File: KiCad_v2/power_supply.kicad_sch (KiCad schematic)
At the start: 41 parts, among them U1 MT3608, U6 MCP73871, U8 TPS54331

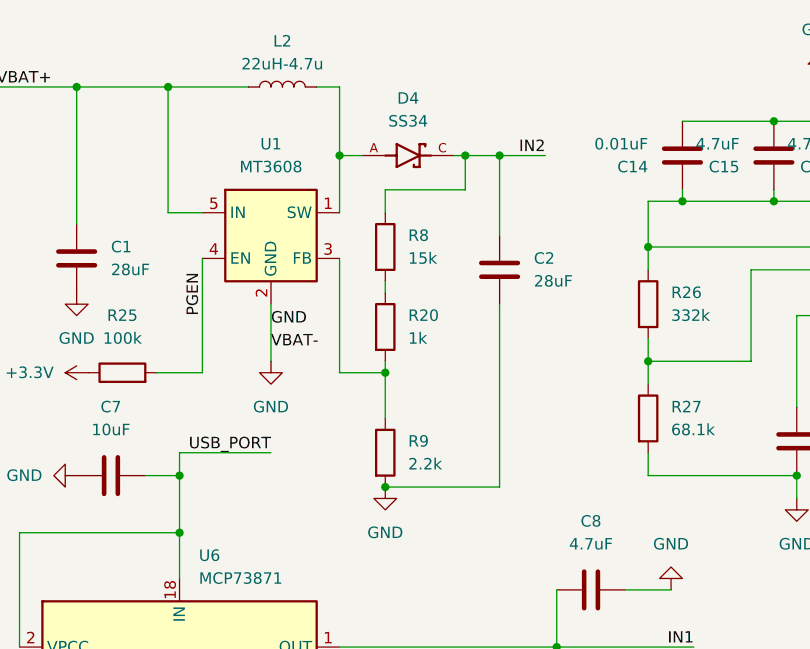
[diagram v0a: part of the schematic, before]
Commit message: feat: agrego 3d de ESP32 Y CM4
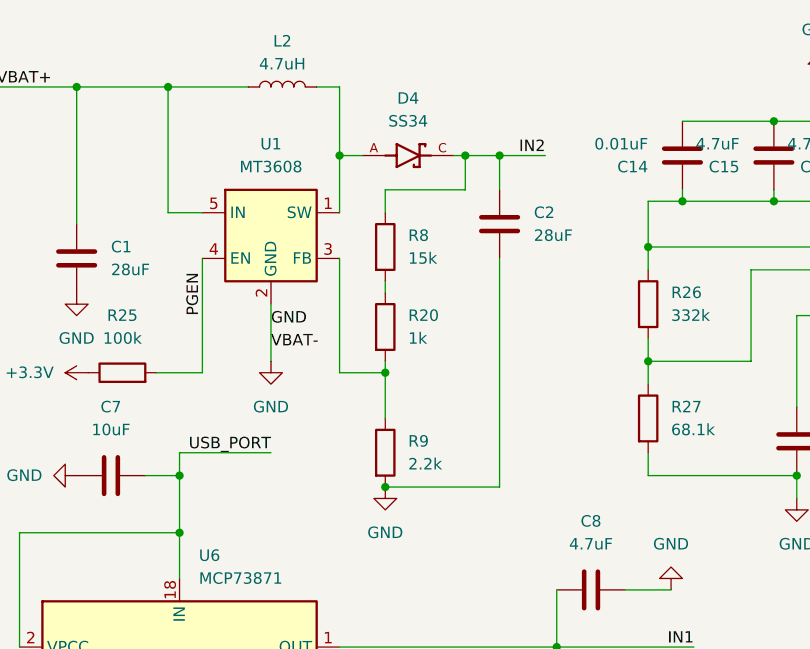
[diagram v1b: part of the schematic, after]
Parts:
- D4: footprint Footprint KiCad:DIOM7959X265N -> Custom_Footprints:DIOM7959X265N
- D5: footprint Footprint KiCad:B340A -> Custom_Footprints:B340A
- L2: value 22uH-4.7u -> 4.7uH
- U8: footprint Footprint KiCad:SOP8 -> Custom_Footprints:SOP8
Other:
- moved on the sheet: C2
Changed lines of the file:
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@@
 	(wire
 		(pts
-			(xy 109.22 88.9) (xy 109.22 109.22)
+			(xy 109.22 83.82) (xy 109.22 109.22)
 		)
 		(stroke
@@
 	(wire
 		(pts
-			(xy 109.22 72.39) (xy 109.22 81.28)
+			(xy 109.22 72.39) (xy 109.22 76.2)
 		)
 		(stroke
@@
 			)
 		)
-		(property "Footprint" "Footprint KiCad:B340A"
+		(property "Footprint" "Custom_Footprints:B340A"
 			(at 200.66 86.36 0)
 			(effects
@@
 			)
 		)
-		(property "Footprint" "Footprint KiCad:DIOM7959X265N"
+		(property "Footprint" "Custom_Footprints:DIOM7959X265N"
 			(at 99.06 72.39 0)
 			(effects
@@
 	(symbol
 		(lib_id "Device:C")
-		(at 109.22 85.09 0)
+		(at 109.22 80.01 0)
 		(unit 1)
 		(exclude_from_sim no)
@@
 		(fields_autoplaced yes)
 		(property "Reference" "C2"
-			(at 113.03 83.8199 0)
+			(at 113.03 78.7399 0)
 			(effects
 				(font
@@
 		)
 		(property "Value" "28uF"
-			(at 113.03 86.3599 0)
+			(at 113.03 81.2799 0)
 			(effects
 				(font
@@
 		)
 		(property "Footprint" "Capacitor_SMD:C_0805_2012Metric"
-			(at 110.1852 88.9 0)
+			(at 110.1852 83.82 0)
 			(effects
 				(font
@@
 		)
 		(property "Datasheet" "~"
-			(at 109.22 85.09 0)
+			(at 109.22 80.01 0)
 			(effects
 				(font
@@
 		)
 		(property "Description" "Unpolarized capacitor"
-			(at 109.22 85.09 0)
+			(at 109.22 80.01 0)
 			(effects
 				(font
@@
 		)
 		(property "Sim.Device" ""
-			(at 109.22 85.09 0)
+			(at 109.22 80.01 0)
 			(effects
 				(font
@@
 			)
 		)
-		(property "Value" "22uH-4.7u"
+		(property "Value" "4.7uH"
 			(at 85.09 62.23 90)
 			(effects
@@
 			)
 		)
-		(property "Footprint" "Footprint KiCad:SOP8"
+		(property "Footprint" "Custom_Footprints:SOP8"
 			(at 168.91 87.63 0)
 			(effects

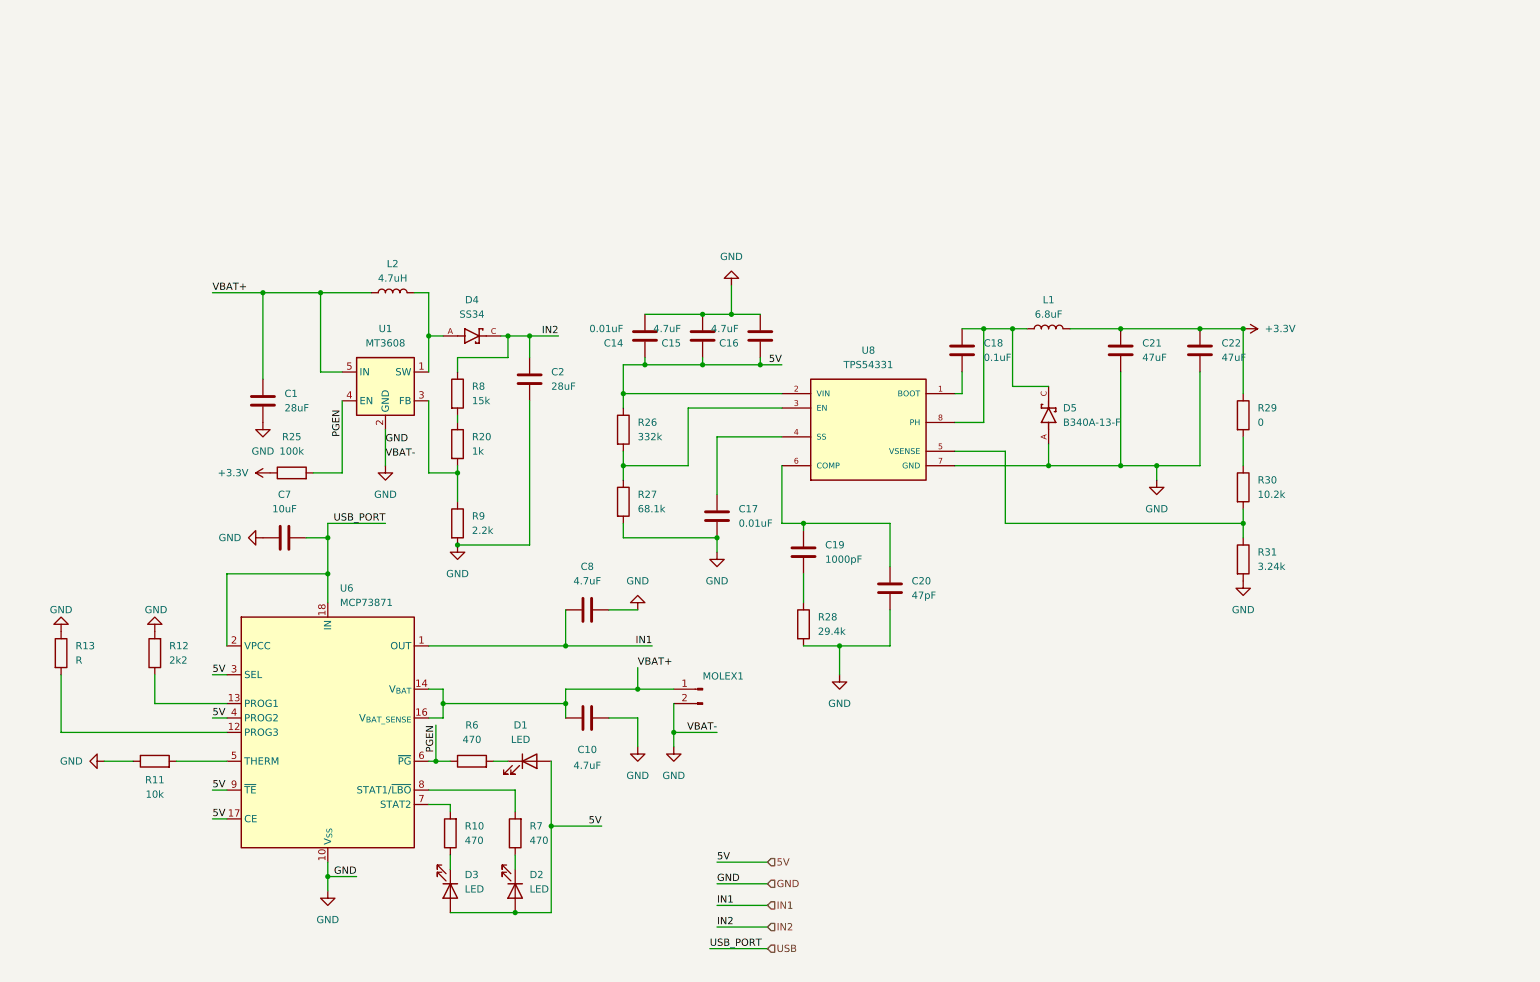
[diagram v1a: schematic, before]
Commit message: agrego step up para 3A con su debido esquematico
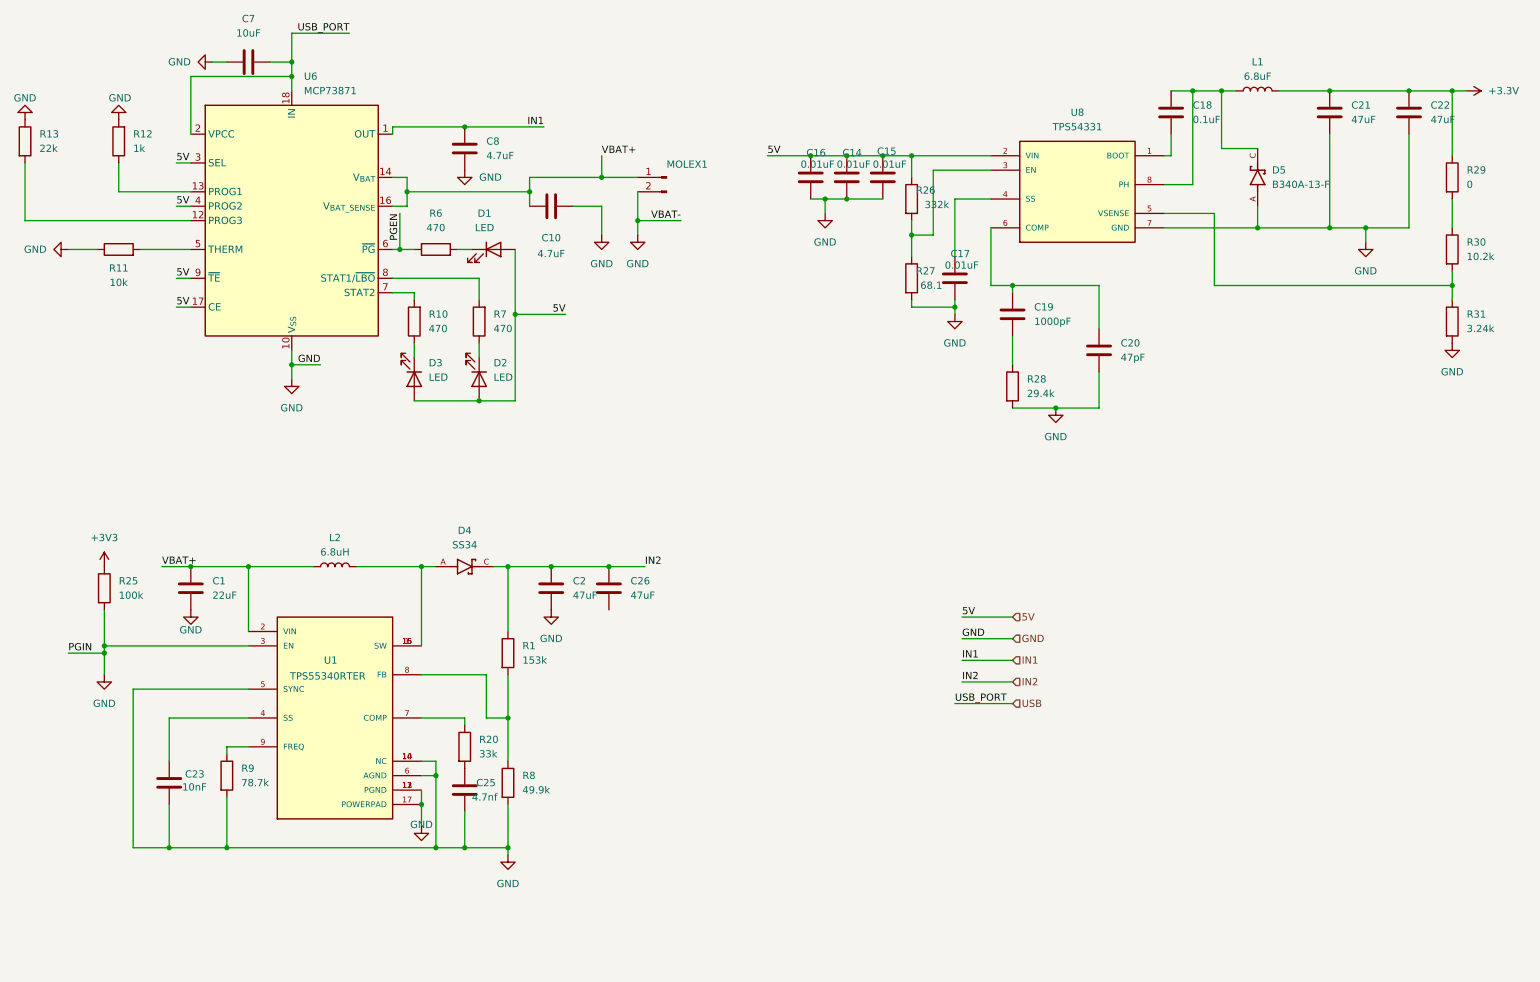
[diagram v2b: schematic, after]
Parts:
- removed U1: MT3608, Package_TO_SOT_SMD:SOT-23-6, symbol Regulator_Switching:MT3608
- added C23: 10nF, Capacitor_SMD:C_0805_2012Metric, symbol Device:C
- added C25: 4.7nf, Capacitor_SMD:C_0805_2012Metric, symbol Device:C
- added C26: 47uF, Capacitor_SMD:C_0805_2012Metric, symbol Device:C
- added R1: 153k, Resistor_SMD:R_0805_2012Metric, symbol Device:R
- added U1: TPS55340RTER, Custom_Footprints:QFN50P300X300X80-17N, symbol TPS55340RTER:TPS55340RTER
- C1: value 28uF -> 22uF
- C15, C16: value 4.7uF -> 0.01uF
- C2: value 28uF -> 47uF
- L1: footprint (none) -> Custom_Footprints:IND_SRP6540-100M
- L2: value 4.7uH -> 6.8uH; footprint (none) -> Custom_Footprints:IND_SRP6540-100M
- R12: value 2k2 -> 1k
- R13: value R -> 22k
- R20: value 1k -> 33k
- R27: value 68.1k -> 68.1
- R8: value 15k -> 49.9k
- R9: value 2.2k -> 78.7k
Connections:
- net +3.3V: no longer R25.1
- net GND: now also C8.2, R25.2, R8.2, C23.2, C25.2, U1.10 (NC), U1.11 (PGND), U1.12 (PGND), U1.13 (PGND), U1.14 (NC), U1.17 (POWERPAD), U1.3 (EN), U1.5 (SYNC), U1.6 (AGND); no longer C8.1
- net IN1: now also C8.1; no longer C8.2
- net IN2: now also C26.1, R1.1; no longer R8.1
- net PGEN: no longer R25.2
- net VBAT+: now also U1.2 (VIN)
- net at R20.1: now also U1.7 (COMP); no longer R8.2
- net at R9.1: now also U1.9 (FREQ); no longer R20.2
- net at D4.A, L2.2: now also U1.1 (SW), U1.15 (SW), U1.16 (SW)
- new net: C23.1, U1.4 (SS)
- new net: R1.2, R8.1, U1.8 (FB)
- new net: C25.1, R20.2
- new net +3V3: R25.1
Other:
- moved on the sheet: C10, C17, C18, C19, C20, C21, C22, C7, C8, D1, D2, D3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

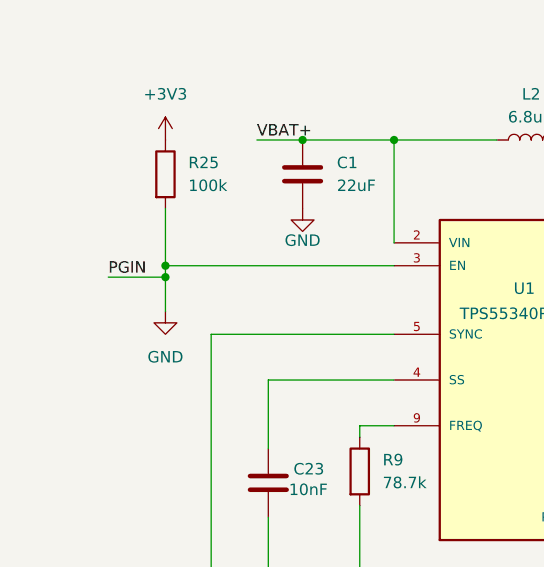
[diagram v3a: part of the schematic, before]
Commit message: Resistencias calculadas, esquematico terminado
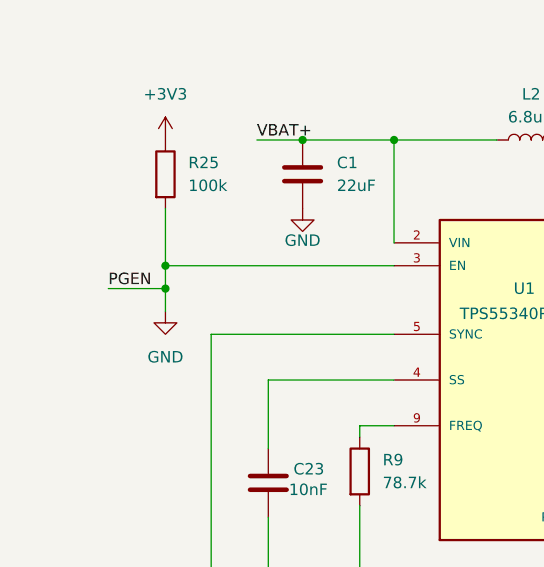
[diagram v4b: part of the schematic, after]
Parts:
- C1, C10, C14, C15, C16, C17, C18, C19, C2, C20, C21, C22, C23, C25, C26, C7, C8: footprint Capacitor_SMD:C_0805_2012Metric -> Capacitor_SMD:C_0603_1608Metric
- D1, D2, D3: footprint LED_SMD:LED_0805_2012Metric -> LED_SMD:LED_0603_1608Metric
- R1, R10, R11, R12, R13, R20, R25, R26, R27, R28, R29, R30, R31, R6, R7, R8, R9: footprint Resistor_SMD:R_0805_2012Metric -> Resistor_SMD:R_0603_1608Metric
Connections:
- net PGEN is gone; now on net GND: R6.1, U6.6 (~{PG})
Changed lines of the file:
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@@
 	)
 	(junction
+		(at 34.29 129.54)
+		(diameter 0)
+		(color 0 0 0 0)
+	)
+	(junction
 		(at 256.54 53.34)
 		(diameter 0)
@@
 	)
 	(junction
-		(at 34.29 128.27)
-		(diameter 0)
-		(color 0 0 0 0)
-	)
-	(junction
 		(at 97.79 35.56)
 		(diameter 0)
@@
 	(wire
 		(pts
-			(xy 34.29 128.27) (xy 34.29 132.08)
-		)
-		(stroke
-			(width 0)
-			(type default)
-		)
-	)
-	(wire
-		(pts
 			(xy 222.25 36.83) (xy 222.25 40.64)
 		)
@@
 	(wire
 		(pts
+			(xy 34.29 127) (xy 34.29 129.54)
+		)
+		(stroke
+			(width 0)
+			(type default)
+		)
+	)
+	(wire
+		(pts
 			(xy 100.33 73.66) (xy 100.33 76.2)
 		)
@@
 	(wire
 		(pts
+			(xy 34.29 129.54) (xy 34.29 132.08)
+		)
+		(stroke
+			(width 0)
+			(type default)
+		)
+	)
+	(wire
+		(pts
 			(xy 184.15 58.42) (xy 184.15 48.26)
 		)
@@
 	(wire
 		(pts
-			(xy 34.29 127) (xy 34.29 128.27)
-		)
-		(stroke
-			(width 0)
-			(type default)
-		)
-	)
-	(wire
-		(pts
 			(xy 59.69 134.62) (xy 39.37 134.62)
 		)
@@
 	(wire
 		(pts
-			(xy 34.29 128.27) (xy 27.94 128.27)
+			(xy 34.29 129.54) (xy 27.94 129.54)
 		)
 		(stroke
@@
 		)
 	)
-	(label "PGIN"
-		(at 27.94 128.27 0)
+	(label "PGEN"
+		(at 27.94 129.54 0)
 		(effects
 			(font
@@
 			)
 		)
-		(property "Footprint" "Capacitor_SMD:C_0805_2012Metric"
+		(property "Footprint" "Capacitor_SMD:C_0603_1608Metric"
 			(at 185.1152 66.04 0)
 			(effects
@@
 			)
 		)
-		(property "Footprint" "Capacitor_SMD:C_0805_2012Metric"
+		(property "Footprint" "Capacitor_SMD:C_0603_1608Metric"
 			(at 50.4952 120.65 0)
 			(effects
@@
 			)
 		)
-		(property "Footprint" "LED_SMD:LED_0805_2012Metric"
+		(property "Footprint" "LED_SMD:LED_0603_1608Metric"
 			(at 100.33 80.01 0)
 			(effects
@@
 			)
 		)
-		(property "Footprint" "Capacitor_SMD:C_0805_2012Metric"
+		(property "Footprint" "Capacitor_SMD:C_0603_1608Metric"
 			(at 113.9952 120.65 0)
 			(effects
@@
 			)
 		)
-		(property "Footprint" "Capacitor_SMD:C_0805_2012Metric"
+		(property "Footprint" "Capacitor_SMD:C_0603_1608Metric"
 			(at 195.2752 72.39 0)
 			(effects
@@
 			)
 		)
-		(property "Footprint" "Resistor_SMD:R_0805_2012Metric"
+		(property "Footprint" "Resistor_SMD:R_0603_1608Metric"
 			(at 54.102 149.86 90)
 			(effects
@@
 			)
 		)
-		(property "Footprint" "Capacitor_SMD:C_0805_2012Metric"
+		(property "Footprint" "Capacitor_SMD:C_0603_1608Metric"
 			(at 172.4152 48.26 0)
 			(effects
@@
 			)
 		)
-		(property "Footprint" "Resistor_SMD:R_0805_2012Metric"
+		(property "Footprint" "Resistor_SMD:R_0603_1608Metric"
 			(at 270.002 57.15 90)
 			(effects
@@
 			)
 		)
-		(property "Footprint" "Capacitor_SMD:C_0805_2012Metric"
+		(property "Footprint" "Capacitor_SMD:C_0603_1608Metric"
 			(at 251.1552 36.83 0)
 			(effects
@@
 			)
 		)
-		(property "Footprint" "LED_SMD:LED_0805_2012Metric"
+		(property "Footprint" "LED_SMD:LED_0603_1608Metric"
 			(at 102.87 57.15 0)
 			(effects
@@
 			)
 		)
-		(property "Footprint" "Resistor_SMD:R_0805_2012Metric"
+		(property "Footprint" "Resistor_SMD:R_0603_1608Metric"
 			(at 174.752 62.23 90)
 			(effects
@@
 			)
 		)
-		(property "Footprint" "Resistor_SMD:R_0805_2012Metric"
+		(property "Footprint" "Resistor_SMD:R_0603_1608Metric"
 			(at 90.678 69.85 90)
 			(effects
@@
 			)
 		)
-		(property "Footprint" "Resistor_SMD:R_0805_2012Metric"
+		(property "Footprint" "Resistor_SMD:R_0603_1608Metric"
 			(at 38.608 38.1 90)
 			(effects
@@
 			)
 		)
-		(property "Footprint" "Capacitor_SMD:C_0805_2012Metric"
+		(property "Footprint" "Capacitor_SMD:C_0603_1608Metric"
 			(at 210.5152 78.74 0)
 			(effects
@@
 			)
 		)
-		(property "Footprint" "Resistor_SMD:R_0805_2012Metric"
+		(property "Footprint" "Resistor_SMD:R_0603_1608Metric"
 			(at 270.002 69.85 90)
 			(effects
@@
 			)
 		)
-		(property "Footprint" "Resistor_SMD:R_0805_2012Metric"
+		(property "Footprint" "Resistor_SMD:R_0603_1608Metric"
 			(at 32.512 116.84 90)
 			(effects
@@
 			)
 		)
-		(property "Footprint" "Resistor_SMD:R_0805_2012Metric"
+		(property "Footprint" "Resistor_SMD:R_0603_1608Metric"
 			(at 92.71 58.928 90)
 			(effects
@@
 			)
 		)
-		(property "Footprint" "Resistor_SMD:R_0805_2012Metric"
+		(property "Footprint" "Resistor_SMD:R_0603_1608Metric"
 			(at 103.632 151.13 90)
 			(effects
@@
 			)
 		)
-		(property "Footprint" "Resistor_SMD:R_0805_2012Metric"
+		(property "Footprint" "Resistor_SMD:R_0603_1608Metric"
 			(at 270.002 44.45 90)
 			(effects
@@
 			)
 		)
-		(property "Footprint" "Capacitor_SMD:C_0805_2012Metric"
+		(property "Footprint" "Capacitor_SMD:C_0603_1608Metric"
 			(at 98.7552 43.18 0)
 			(effects
@@
 			)
 		)
-		(property "Footprint" "Resistor_SMD:R_0805_2012Metric"
+		(property "Footprint" "Resistor_SMD:R_0603_1608Metric"
 			(at 174.752 48.26 90)
 			(effects
@@
 			)
 		)
-		(property "Footprint" "Capacitor_SMD:C_0805_2012Metric"
+		(property "Footprint" "Capacitor_SMD:C_0603_1608Metric"
 			(at 116.84 48.5648 0)
 			(effects
@@
 			)
 		)
-		(property "Footprint" "LED_SMD:LED_0805_2012Metric"
+		(property "Footprint" "LED_SMD:LED_0603_1608Metric"
 			(at 88.9 80.01 0)
 			(effects
@@
 			)
 		)
-		(property "Footprint" "Capacitor_SMD:C_0805_2012Metric"
+		(property "Footprint" "Capacitor_SMD:C_0603_1608Metric"
 			(at 46.6852 154.94 0)
 			(effects
@@
 			)
 		)
-		(property "Footprint" "Capacitor_SMD:C_0805_2012Metric"
+		(property "Footprint" "Capacitor_SMD:C_0603_1608Metric"
 			(at 124.1552 120.65 0)
 			(effects
@@
 			)
 		)
-		(property "Footprint" "Resistor_SMD:R_0805_2012Metric"
+		(property "Footprint" "Resistor_SMD:R_0603_1608Metric"
 			(at 102.108 69.85 90)
 			(effects
@@
 			)
 		)
-		(property "Footprint" "Capacitor_SMD:C_0805_2012Metric"
+		(property "Footprint" "Capacitor_SMD:C_0603_1608Metric"
 			(at 63.5 23.1648 0)
 			(effects
@@
 			)
 		)
-		(property "Footprint" "Resistor_SMD:R_0805_2012Metric"
+		(property "Footprint" "Resistor_SMD:R_0603_1608Metric"
 			(at 18.542 38.1 90)
 			(effects
@@
 			)
 		)
-		(property "Footprint" "Capacitor_SMD:C_0805_2012Metric"
+		(property "Footprint" "Capacitor_SMD:C_0603_1608Metric"
 			(at 265.1252 36.83 0)
 			(effects
@@
 			)
 		)
-		(property "Footprint" "Resistor_SMD:R_0805_2012Metric"
+		(property "Footprint" "Resistor_SMD:R_0603_1608Metric"
 			(at 103.632 128.27 90)
 			(effects
@@
 			)
 		)
-		(property "Footprint" "Capacitor_SMD:C_0805_2012Metric"
+		(property "Footprint" "Capacitor_SMD:C_0603_1608Metric"
 			(at 166.0652 48.26 0)
 			(effects
@@
 			)
 		)
-		(property "Footprint" "Resistor_SMD:R_0805_2012Metric"
+		(property "Footprint" "Resistor_SMD:R_0603_1608Metric"
 			(at 36.83 58.928 90)
 			(effects
@@
 			)
 		)
-		(property "Footprint" "Capacitor_SMD:C_0805_2012Metric"
+		(property "Footprint" "Capacitor_SMD:C_0603_1608Metric"
 			(at 98.7552 156.21 0)
 			(effects
@@
 			)
 		)
-		(property "Footprint" "Capacitor_SMD:C_0805_2012Metric"
+		(property "Footprint" "Capacitor_SMD:C_0603_1608Metric"
 			(at 159.7152 48.26 0)
 			(effects
@@
 			)
 		)
-		(property "Footprint" "Resistor_SMD:R_0805_2012Metric"
+		(property "Footprint" "Resistor_SMD:R_0603_1608Metric"
 			(at 96.012 144.78 90)
 			(effects
@@
 			)
 		)
-		(property "Footprint" "Resistor_SMD:R_0805_2012Metric"
+		(property "Footprint" "Resistor_SMD:R_0603_1608Metric"
 			(at 192.532 81.28 90)
 			(effects
@@
 			)
 		)
-		(property "Footprint" "Capacitor_SMD:C_0805_2012Metric"
+		(property "Footprint" "Capacitor_SMD:C_0603_1608Metric"
 			(at 223.2152 36.83 0)
 			(effects
